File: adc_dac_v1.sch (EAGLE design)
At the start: 127 parts, among them IC1 OPA1662, IC3 ADA4610-2, U1 AD7960BCPZ-RL7, U10 UA78M05CDCYR, U11 LP5907MFX-1.8/NOPB, U12 ADP2300AUJZ-R7, U13 LM317LIPKG3, U14 LM317LIPKG3, U15 LM337LMX/NOPB, U16 ADR395AUJZ-REEL7, U17 MAX5802BAUB+, U18 LM337LMX/NOPB, U19 MAX6070BAUT21+T, U2 AD5453YRMZ-REEL7, U20 CD40106BM96, U3 ADA4932-1YCPZ-R7, U31 BC857BS-13-F, U4 NLSX3018DTR2G, U5 NLSX3018DTR2G, U6 ADS7952SRHBT, U7 OPA202, U8 REF5025AIDR, U9 ADP150AUJZ-3.3-R7, X1 BU-SMA-G, X2 BU-SMA-G

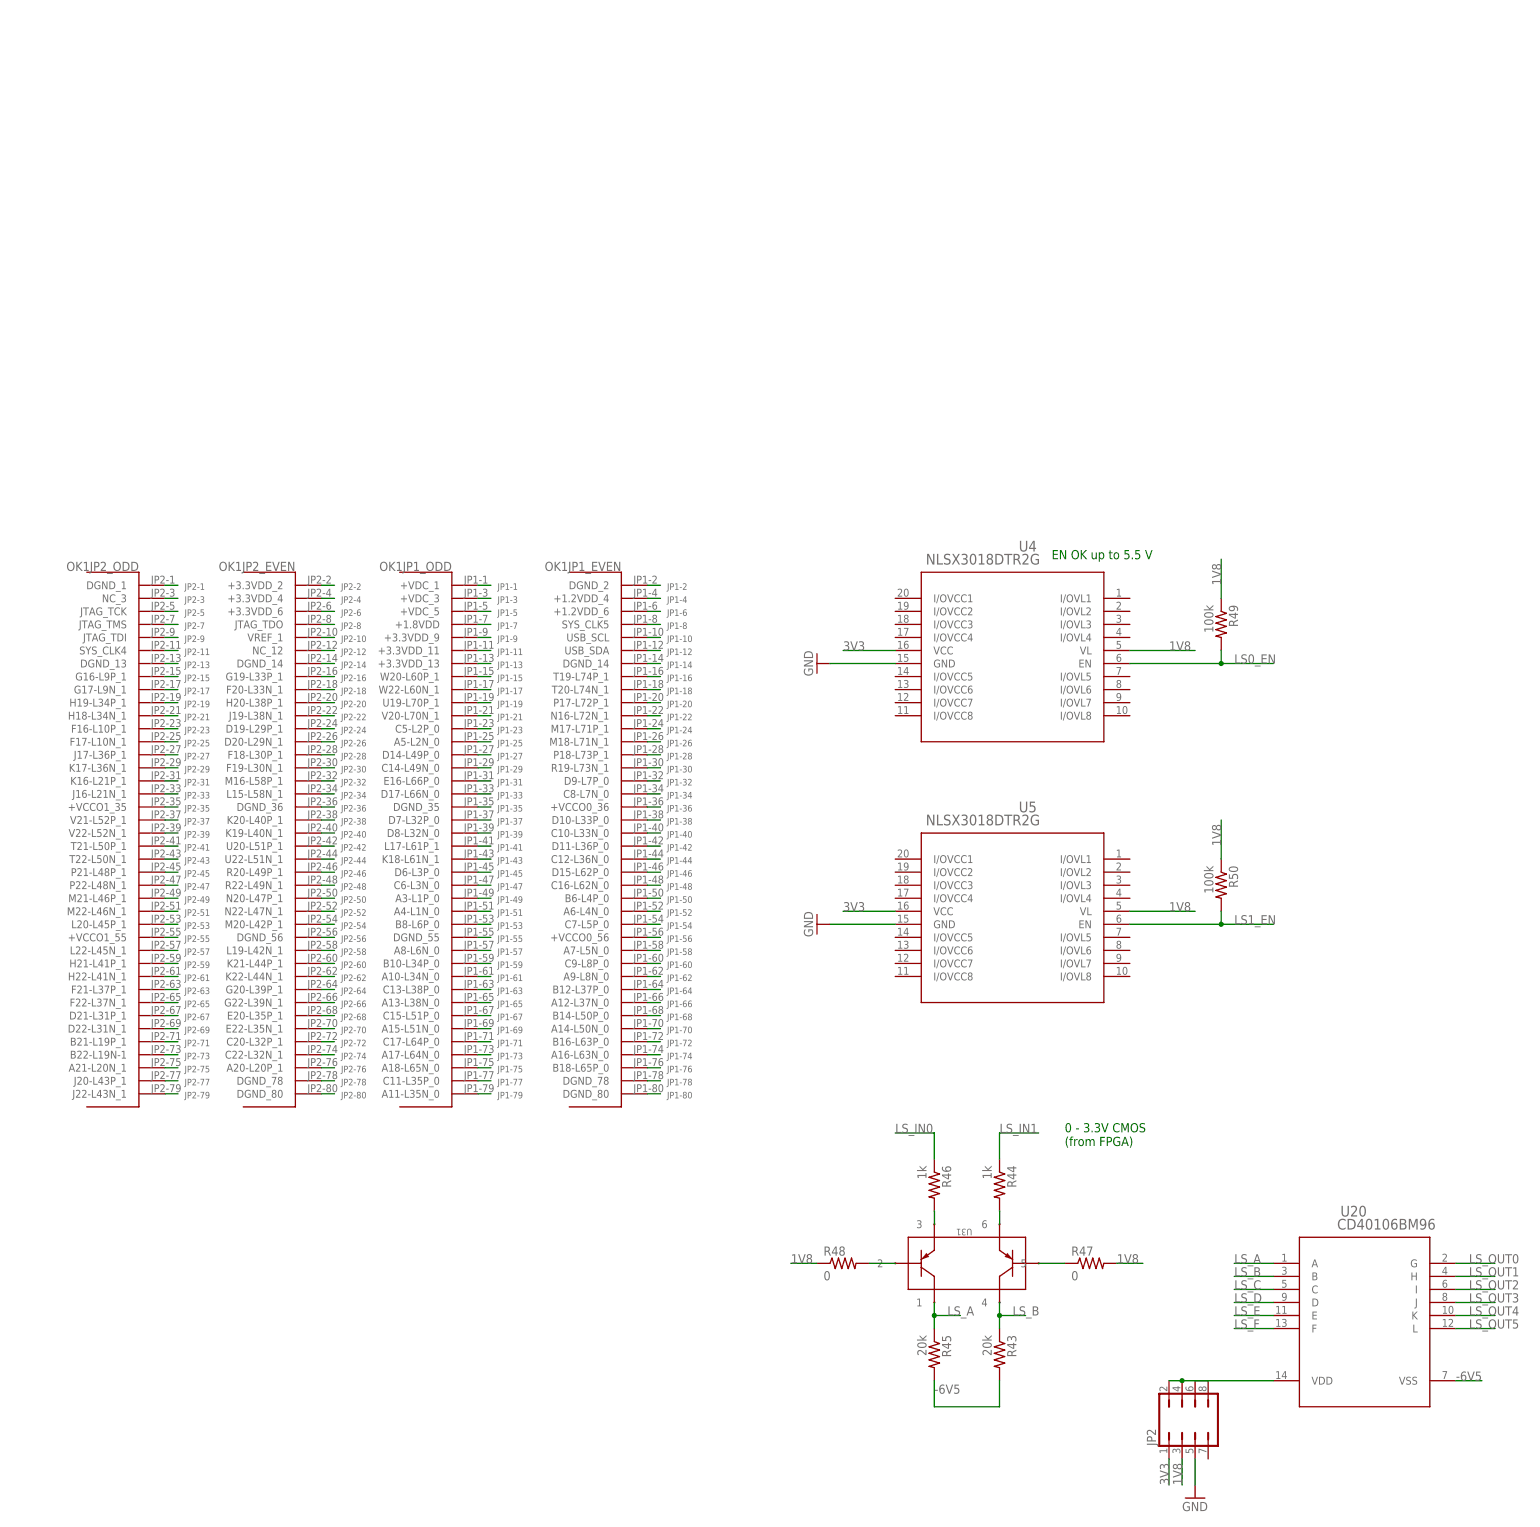
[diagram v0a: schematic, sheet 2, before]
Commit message: added frames, initial brd placement
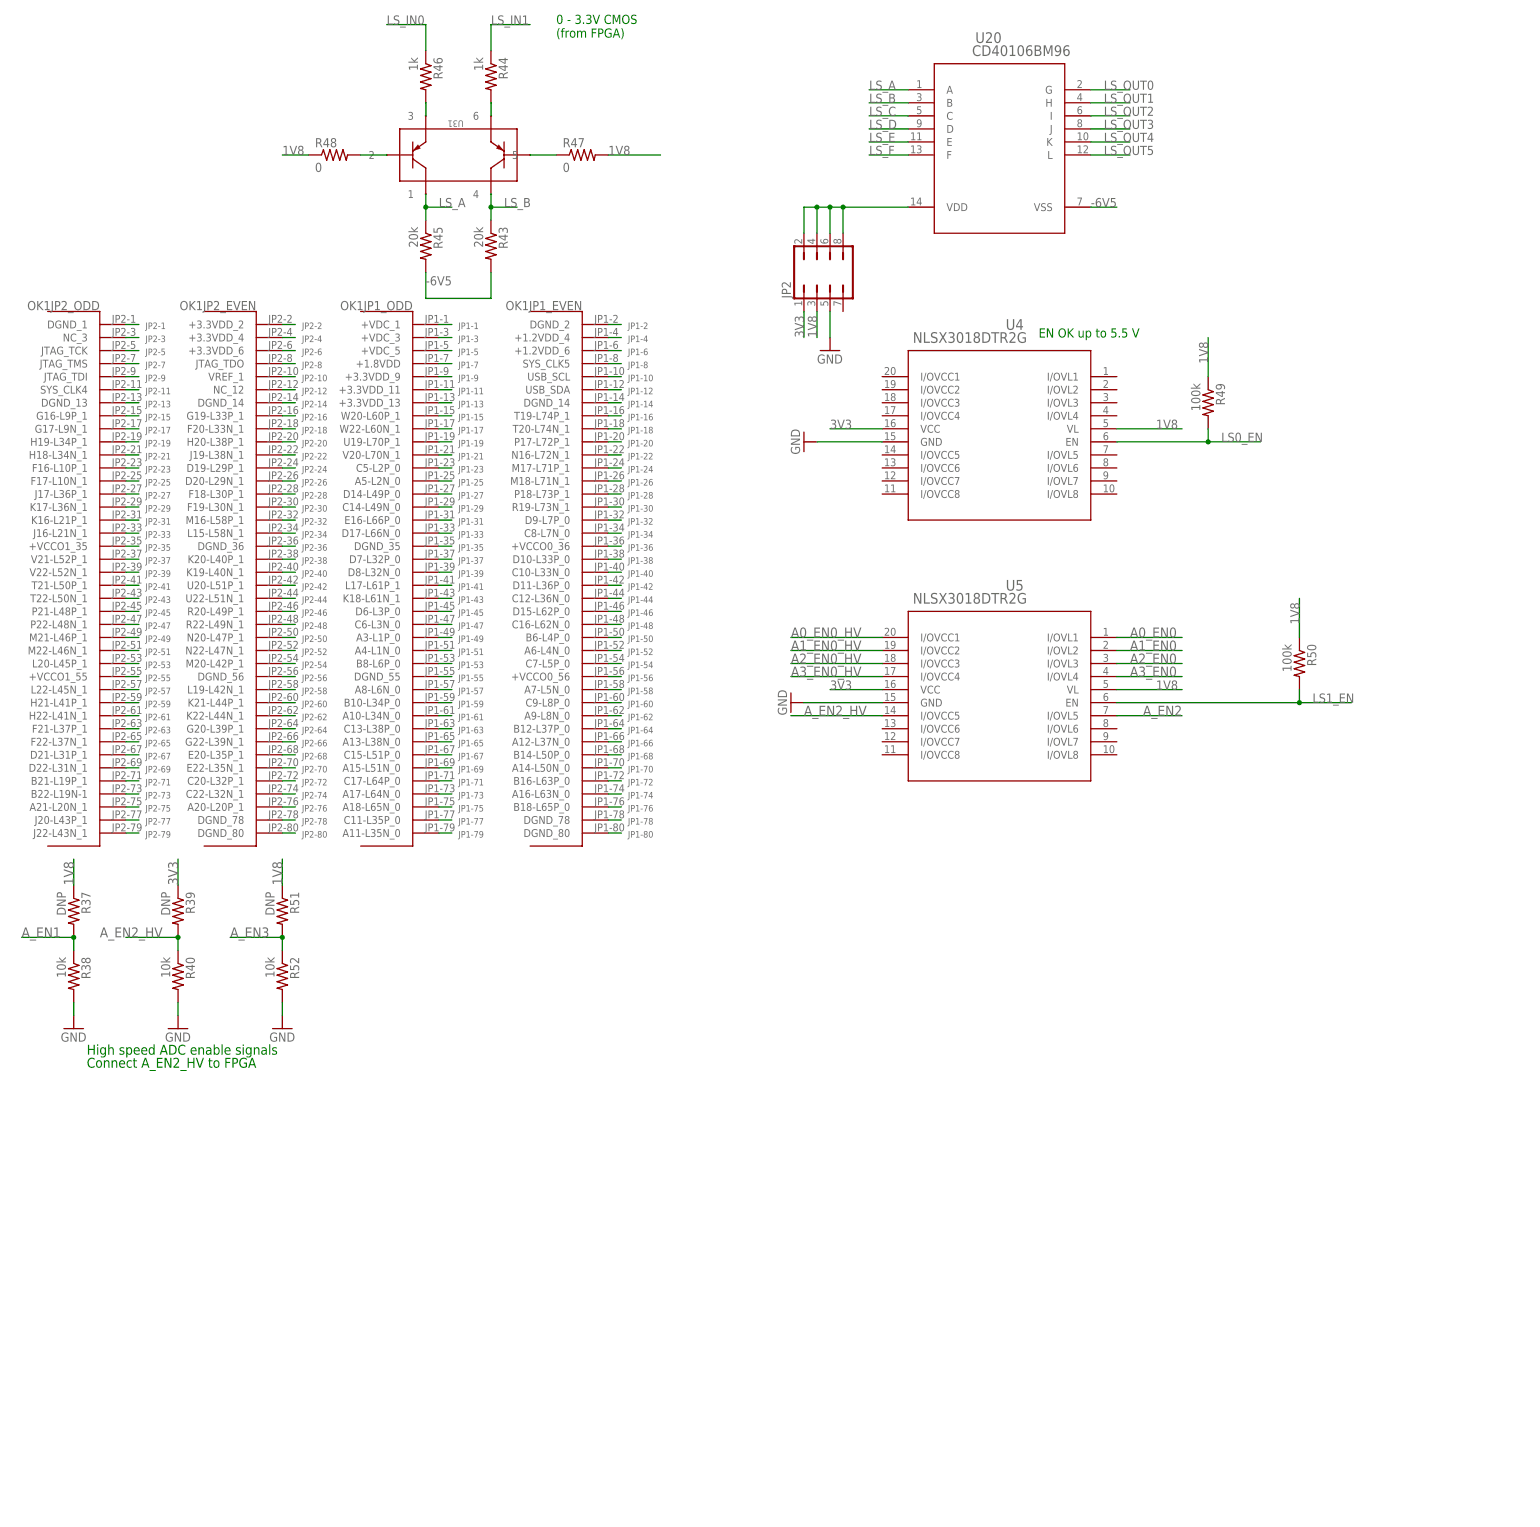
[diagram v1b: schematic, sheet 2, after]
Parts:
- added R37, R39, R51: DNP, rcl:R-US_R0603
- added R38, R40, R52: 10k, rcl:R-US_R0603
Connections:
- net CLK+ renamed A0_CLK+
- net CLK- renamed A0_CLK-
- net CNV+ renamed A0_CNV+
- net CNV- renamed A0_CNV-
- net CSB renamed D0_CSB
- net D+ renamed A0_D+
- net D- renamed A0_D-
- net DACS_0 renamed DS_OUT0
- net DACS_1 renamed DS_OUT1
- net DACS_CLRB renamed DS_CLRB
- net DACS_SCL renamed DS_SCL
- net DACS_SDA renamed DS_SDA
- net DCO+ renamed A0_DCO+
- net DCO- renamed A0_DCO-
- net DIFF_IN+ renamed A0_AMP_IN+
- net DIFF_IN- renamed A0_AMP_IN-
- net IN+ renamed A0_IN+
- net IN- renamed A0_IN-
- net OUT renamed D0_OUT
- net SCLK renamed D0_SCLK
- net SDI renamed D0_SDI
- net VCM renamed A0_VCM
- net VREF_BUF renamed D0_VREF_BUF
- removed net EN0: U1.EN0
- removed net EN1: U1.EN1
- removed net EN2: U1.EN2
- removed net EN3: U1.EN3
- removed net N$40: JP2.2, JP2.4, U20.VDD
- removed net N$41: JP2.6, JP2.8
- new net A0_EN0: U1.EN0, U5.I/OVL1
- new net A0_EN0_HV: U5.I/OVCC1
- new net A1_EN0: U5.I/OVL2
- new net A1_EN0_HV: U5.I/OVCC2
- new net A2_EN0: U5.I/OVL3
- new net A2_EN0_HV: U5.I/OVCC3
- new net A3_EN0: U5.I/OVL4
- new net A3_EN0_HV: U5.I/OVCC4
- new net A_EN1: R37.2, R38.1, U1.EN1
- new net A_EN2: U1.EN2, U5.I/OVL5
- new net A_EN2_HV: R39.2, R40.1, U5.I/OVCC5
- new net A_EN3: R51.2, R52.1, U1.EN3
- new net N$33: JP2.2, JP2.4, JP2.6, JP2.8, U20.VDD
- net 1V8: now also R37.1, R51.1
- net 3V3: now also R39.1
- net 5V: now also U10.OUT; no longer U10.IN
- net 7V5_IN: now also U10.IN; no longer U10.OUT
- net GND: now also R38.2, R40.2, R52.2, U10.COM2
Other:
- note added: "Connect A_EN2_HV to FPGA"
- note added: "High speed ADC enable signals"
- note added: "Slow DAC for offset voltages, etc."
- moved on the sheet: C1, C10, C11, C12, C13, C14, C15, C16, C17, C18, C19, C2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

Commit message: updates before copying the ADC
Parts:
- added C52, C53, C54: 0.1u, rcl:C-USC0603
- added H1, H2, H3, H4: MOUNT-HOLE3.0, holes:MOUNT-HOLE3.0
- added J1: PJ-202AH, open_covg:PJ-202AH
- added J2: PJ-002B, open_covg:PJ-002B
- C12, C13: device rcl:C-USC0805 -> rcl:C-USC0603
- U17: value MAX5802BAUB+ -> MAX5802
- U2: value AD5453YRMZ-REEL7 -> AD5453
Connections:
- removed net N$22: C21.1, U8.VIN
- net 18V_IN: now also J2.1
- net 3V3: now also C52.1
- net 5V: now also C21.1, C53.1, U8.VIN
- net 7V5_IN: now also J1.1
- net AMP_PWR-: now also C54.1; no longer C18.2
- net GND: now also C18.2, C52.2, C53.2, C54.2, J1.2, J2.2
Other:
- note added: "7.5 V External Supply 18 V External Supply"
- note added: "Alternative signal connection or ground the inputs"
- note added: "These are global (for all ADC channels) EN0 is the only signal that needs FPGA control per ADC channel."
- note added: "VSS - VDD to FET switches on analog board"
- moved on the sheet: C44, U16

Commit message: added libraries from Autodesk downloaded; routing near completion
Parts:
- added C55, C69, C83: 100p, rcl:C-USC0603
- added C56, C66, C70, C80, C84, C94: 10u, rcl:C-USC0603
- added C57, C58, C59, C60, C61, C64, C65, C67, C68, C71, C72, C73, C74, C75, C78, C79, C81, C82, C85, C86, C87, C88, C89, C92, C93, C95, C96: 0.1u, rcl:C-USC0603
- added C62, C63, C76, C77, C90, C91: DNP, rcl:C-USC0603
- added J3: 2-406541-3, open_covg:2-406541-3
- added JP3, JP4: (no value), pinhead-2:PINHD-1X04_2.54-SMD
- added P1: M-2X06-87759_M, con-headers-jp:M-2X06-87759_M
- added P2: M-2X10-87759_M, con-headers-jp:M-2X10-87759_M
- added R100, R101, R63, R64, R88, R89: 33, rcl:R-US_R0603
- added R53, R54, R55, R56, R78, R79, R80, R81, R90, R91, R92, R93: 499, rcl:R-US_R0603
- added R57, R58, R82, R83, R94, R95: 100, rcl:R-US_R0603
- added R59, R62, R84, R87, R96, R99: DNP, rcl:R-US_R0603
- added R60, R61, R65, R70, R71, R76, R77, R85, R86, R97, R98: 0, rcl:R-US_R0603
- added R66, R68, R72, R74: 20k, rcl:R-US_R0603
- added R67, R69, R73, R75: 1k, rcl:R-US_R0603
- added U$1: 0532611471_PICOBLADE, open_covg:0532611471_PICOBLADE
- added U21, U25, U27: ADA4932-1YCPZ-R7, AD7960:ADA4932-1YCPZ-R7
- added U22, U26, U28: AD7960BCPZ-RL7, open_covg:AD7960BCPZ-RL7
- added U23, U24: BC857BS-13-F, open_covg:HN1A01FU-YLFCT
- added X3, X4, X5, X6, X7, X8: BU-SMA-G, con-coax:BU-SMA-G
- added X9: 1365-10, con-leotronics:1365-10
- JP1: device pinhead:PINHD-1X4 -> pinhead-2:PINHD-1X04_2.54-SMD
- JP2: device jumper:JP4Q -> pinhead-2:PINHD-1X04_2.54-SMD
- R21: value 1k -> 2k
- R22: value 2k -> 1k
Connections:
- net N$1 renamed D0_IOUT
- removed net JP2-12: OK1JP2_EVEN.NC_12
- removed net JP2-3: OK1JP2_ODD.NC_3
- new net 15V: U16.SHDNB, U16.VIN
- new net A1_AMP_IN+: JP1.1, R60.1, X3.1
- new net A1_AMP_IN-: JP1.4, R61.1, X4.1
- new net A1_CLK+: R58.1, U22.CLK+
- new net A1_CLK-: R58.2, U22.CLK-
- new net A1_CNV+: R57.2, U22.CNV+
- new net A1_CNV-: R57.1, U22.CNV-
- new net A1_D+: U22.D+
- new net A1_D-: U22.D-
- new net A1_DCO+: U22.DCO+
- new net A1_DCO-: U22.DCO-
- new net A1_IN+: C55.2, R64.2, U22.IN+
- new net A1_IN-: C55.1, R63.2, U22.IN-
- new net A1_VCM: C56.1, U21.VOCM, U22.VCM
- new net A2_AMP_IN+: JP3.1, R85.1, X5.1
- new net A2_AMP_IN-: JP3.4, R86.1, X6.1
- new net A2_CLK+: R83.1, U26.CLK+
- new net A2_CLK-: R83.2, U26.CLK-
- new net A2_CNV+: R82.2, U26.CNV+
- new net A2_CNV-: R82.1, U26.CNV-
- new net A2_D+: U26.D+
- new net A2_D-: U26.D-
- new net A2_DCO+: U26.DCO+
- new net A2_DCO-: U26.DCO-
- new net A2_IN+: C69.2, R89.2, U26.IN+
- new net A2_IN-: C69.1, R88.2, U26.IN-
- new net A2_VCM: C70.1, U25.VOCM, U26.VCM
- new net A3_AMP_IN+: JP4.1, R97.1, X7.1
- new net A3_AMP_IN-: JP4.4, R98.1, X8.1
- new net A3_CLK+: R95.1, U28.CLK+
- new net A3_CLK-: R95.2, U28.CLK-
- new net A3_CNV+: R94.2, U28.CNV+
- new net A3_CNV-: R94.1, U28.CNV-
- new net A3_D+: U28.D+
- new net A3_D-: U28.D-
- new net A3_DCO+: U28.DCO+
- new net A3_DCO-: U28.DCO-
- new net A3_IN+: C83.2, R101.2, U28.IN+
- new net A3_IN-: C83.1, R100.2, U28.IN-
- new net A3_VCM: C84.1, U27.VOCM, U28.VCM
- new net GPIO_1V8_0: U5.I/OVL6
- new net GPIO_1V8_1: U5.I/OVL7
- new net GPIO_1V8_2: U5.I/OVL8
- new net GPIO_3V3_0: U5.I/OVCC6
- new net GPIO_3V3_1: U5.I/OVCC7
- new net GPIO_3V3_2: U5.I/OVCC8
- new net LS_IN2: R69.1
- new net LS_IN3: R67.1
- new net LS_IN4: R75.1
- new net LS_IN5: R73.1
- new net N$22: R65.2, U6.GPIO
- new net N$221: R53.1, R55.2, U21.IN+
- new net N$2212: R78.1, R80.2, U25.IN+
- new net N$2213: R90.1, R92.2, U27.IN+
- new net N$36: R71.2, U23.2
- new net N$361: R53.2, U21.FB-
- new net N$3612: R78.2, U25.FB-
- new net N$3613: R90.2, U27.FB-
- new net N$401: R54.1, R56.2, U21.IN-
- new net N$4012: R79.1, R81.2, U25.IN-
- new net N$4013: R91.1, R93.2, U27.IN-
- new net N$41: R70.1, U23.5
- new net N$411: R54.2, U21.FB+
- new net N$4112: R79.2, U25.FB+
- new net N$4113: R91.2, U27.FB+
- new net N$42: R69.2, U23.3
- new net N$421: C63.1, R55.1, R60.2, R62.1
- new net N$4212: C77.1, R80.1, R85.2, R87.1
- new net N$4213: C91.1, R92.1, R97.2, R99.1
- new net N$44: R67.2, U23.6
- new net N$441: C62.1, R56.1, R59.2, R61.2
- new net N$4412: C76.1, R81.1, R84.2, R86.2
- new net N$4413: C90.1, R93.1, R96.2, R98.2
- new net N$45: R77.2, U24.2
- new net N$451: R63.1, U21.OUT-
- new net N$4512: R88.1, U25.OUT-
- new net N$4513: R100.1, U27.OUT-
- new net N$46: R76.1, U24.5
- new net N$461: R64.1, U21.OUT+
- new net N$4612: R89.1, U25.OUT+
- new net N$4613: R101.1, U27.OUT+
- new net N$48: R73.2, U24.6
- net -6V5: now also R66.2, R68.2, R72.2, R74.2
- net 1V8: now also C57.1, C60.1, C65.1, C71.1, C74.1, C79.1, C85.1, C88.1, C93.1, R70.2, R71.1, R76.2, R77.1, U22.VDD2, U22.VDD2_2, U22.VDD2_3, U22.VIO, U26.VDD2, U26.VDD2_2, U26.VDD2_3, U26.VIO, U28.VDD2, U28.VDD2_2, U28.VDD2_3, U28.VIO, X9-3.S; no longer JP2.3
- net 2V048_REF: now also C66.1, C67.1, C80.1, C81.1, C94.1, C95.1, U22.REF, U22.REF_2, U22.REF_3, U22.REF_4, U26.REF, U26.REF_2, U26.REF_3, U26.REF_4, U28.REF, U28.REF_2, U28.REF_3, U28.REF_4
- net 3V3: now also X9-1.S; no longer JP2.1
- net 5V: now also C58.1, C59.1, C61.1, C72.1, C73.1, C75.1, C86.1, C87.1, C89.1, U22.VDD1, U22.VDD1_2, U22.VDD1_3, U26.VDD1, U26.VDD1_2, U26.VDD1_3, U28.VDD1, U28.VDD1_2, U28.VDD1_3, U6.VA+_2
- net A0_AMP_IN+: now also JP2.1; no longer JP1.1
- net A0_AMP_IN-: now also JP2.4; no longer JP1.4
- net A1_EN0: now also U22.EN0
- net A2_EN0: now also U26.EN0
- net A3_EN0: now also U28.EN0
- net AMP_PWR+: now also C64.1, C78.1, C92.1, U21.PD, U21.VS+, U21.VS+_2, U21.VS+_3, U21.VS+_4, U25.PD, U25.VS+, U25.VS+_2, U25.VS+_3, U25.VS+_4, U27.PD, U27.VS+, U27.VS+_2, U27.VS+_3, U27.VS+_4; no longer U16.SHDNB, U16.VIN
- net AMP_PWR-: now also C68.1, C82.1, C96.1, U21.VS-, U21.VS-_2, U21.VS-_3, U21.VS-_4, U25.VS-, U25.VS-_2, U25.VS-_3, U25.VS-_4, U27.VS-, U27.VS-_2, U27.VS-_3, U27.VS-_4
- net A_EN1: now also U22.EN1, U26.EN1, U28.EN1
- net A_EN2: now also U22.EN2, U26.EN2, U28.EN2
- net A_EN3: now also U22.EN3, U26.EN3, U28.EN3
- net D0_OUT: now also J3.1
- net GND: now also C56.2, C57.2, C58.2, C59.2, C60.2, C61.2, C62.2, C63.2, C64.2, C65.2, C66.2, C67.2, C68.2, C70.2, C71.2, C72.2, C73.2, C74.2, C75.2, C76.2, C77.2, C78.2, C79.2, C80.2, C81.2, C82.2, C84.2, C85.2, C86.2, C87.2, C88.2, C89.2, C90.2, C91.2, C92.2, C93.2, C94.2, C95.2, C96.2, J3.2, JP2.2, JP2.3, JP3.2, JP3.3, JP4.2, JP4.3, P1.10, P1.12, P1.2, P1.4, P1.6, P1.8, R59.1, R62.2, R84.1, R87.2, R96.1, R99.2, U21.EPAD, U22.EPAD, U22.GND, U22.GND_2, U22.REFIN, U22.REF_GND, U22.REF_GND_2, U22.REF_GND_3, U25.EPAD, U26.EPAD, U26.GND, U26.GND_2, U26.REFIN, U26.REF_GND, U26.REF_GND_2, U26.REF_GND_3, U27.EPAD, U28.EPAD, U28.GND, U28.GND_2, U28.REFIN, U28.REF_GND, U28.REF_GND_2, U28.REF_GND_3, X3.2, X4.2, X5.2, X6.2, X7.2, X8.2, X9-5.S; no longer JP2.5
- net LS_C: now also R68.1
- net LS_D: now also R66.1, U23.4
- net LS_E: now also R74.1
- net LS_F: now also R72.1, U24.4
- net LS_OUT0: now also P1.1
- net LS_OUT1: now also P1.3
- net LS_OUT2: now also P1.5
- net LS_OUT3: now also P1.7
- net LS_OUT4: now also P1.9
- net LS_OUT5: now also P1.11
- net N$33: now also X9-2.S, X9-4.S, X9-6.S, X9-8.S; no longer JP2.2, JP2.4, JP2.6, JP2.8
- net N$47: now also R75.2, U24.3; no longer U6.VA+_2
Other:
- note added: "16.7 MHz GBW x1.5 for +/-15V output"
- note added: "Pairs: 1,2; 3,6; 4,5; 7,8"
- note added: "VA+ analog supply. 5V allows Range 2: VREF*2 VBD+ is digital I/O supply = 3.3V REF from 2V-3V"
- note added: "VREF buffer 9 kOhm VREF input resistance Gain to 10 V (AD5453 max is 12 V) 22 MHz gain-bandwidth"
- note removed: "16.7 MHz GBW"
- note removed: "VA+ analog supply. 5V allows Range 2: VREF*2 VBD+ is digital I/O supply REF from 2V-3V"
- note removed: "VREF buffer 9 kOhm VREF input resistance Gain to 10 V (AD5443 max is 12 V) 22 MHz gain-bandwidth"

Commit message: duplicating the high-speed DAC block
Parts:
- added C100, C101, C103, C104, C98: 0.1u, rcl:C-USC0603
- added C102: 2p, rcl:C-USC0603
- added C97, C99: DNP, rcl:C-USC0603
- added IC2: ADA4610-2, analog-devices:ADA4692-2R
- added IC4: OPA1662, open_covg:OPA1662
- added R102, R103, R107: 0, rcl:R-US_R0603
- added R104: 10k, rcl:R-US_R0603
- added R105, R106: 20k, rcl:R-US_R0603
- added R108, R109, R111: 1k, rcl:R-US_R0603
- added R110: 2k, rcl:R-US_R0603
- added U29: AD5453, open_covg:AD5453YRMZ-REEL7
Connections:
- new net D1_CSB: U29.SYNCB
- new net D1_IOUT: C102.1, IC4B.IN+, U29.IOUT1
- new net D1_OUT: C99.1, R103.2
- new net D1_SCLK: U29.SCLK
- new net D1_SDI: U29.SDIN
- new net D1_VREF_BUF: C97.1, R102.2, R106.1, U29.VREF
- new net N$10D1: IC2B.IN-, R110.2, R111.1
- new net N$1D1: IC4B.OUT, R104.1, R107.2
- new net N$25D1: IC4A.OUT, R102.1, R108.2
- new net N$2D1: C102.2, R107.1, U29.RFB
- new net N$3D1: IC2A.IN+, R104.2, R105.1, R106.2
- new net N$5D1: IC2A.OUT, IC2B.IN+, R105.2
- new net N$7D1: IC4A.IN-, R108.1, R109.2
- new net N$8D1: IC2B.OUT, R103.1, R110.1
- net +15V: now also C100.1, C104.1, IC2P.V+, IC4P.V+
- net -15V: now also C101.1, C103.1, IC2P.V-, IC4P.V-
- net 3V3: now also C98.1, U29.VDD
- net 5V_REF: now also IC4A.IN+
- net GND: now also C100.2, C101.2, C103.2, C104.2, C97.2, C98.2, C99.2, IC2A.IN-, IC4B.IN-, R109.1, R111.2, U29.GND
